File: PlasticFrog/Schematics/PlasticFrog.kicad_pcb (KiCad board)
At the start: 2 copper layers, 87.3 x 90.1 mm, 210 parts, among them J1 USB_A, J2 Conn_01x04, J3 Conn_01x05, U1 CH552T

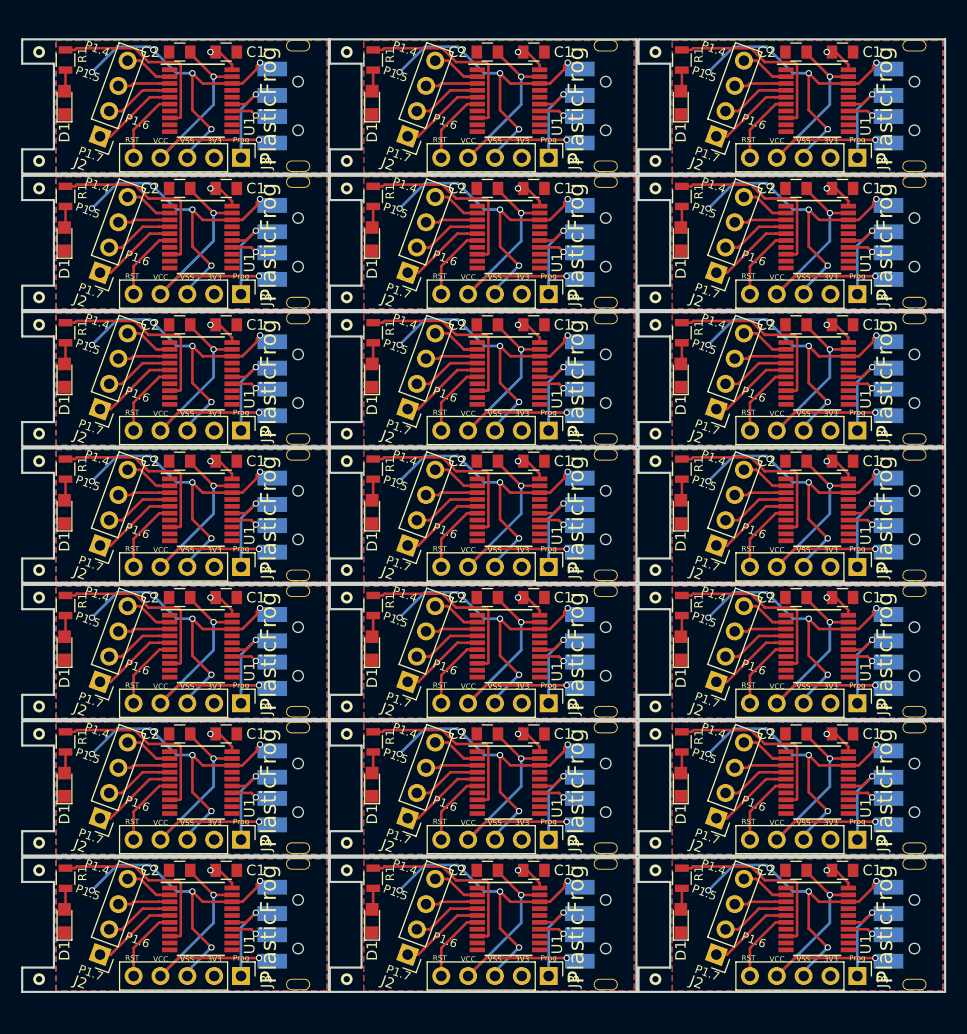
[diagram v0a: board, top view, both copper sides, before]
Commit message: Cant believe I had D+ and D- mixed...
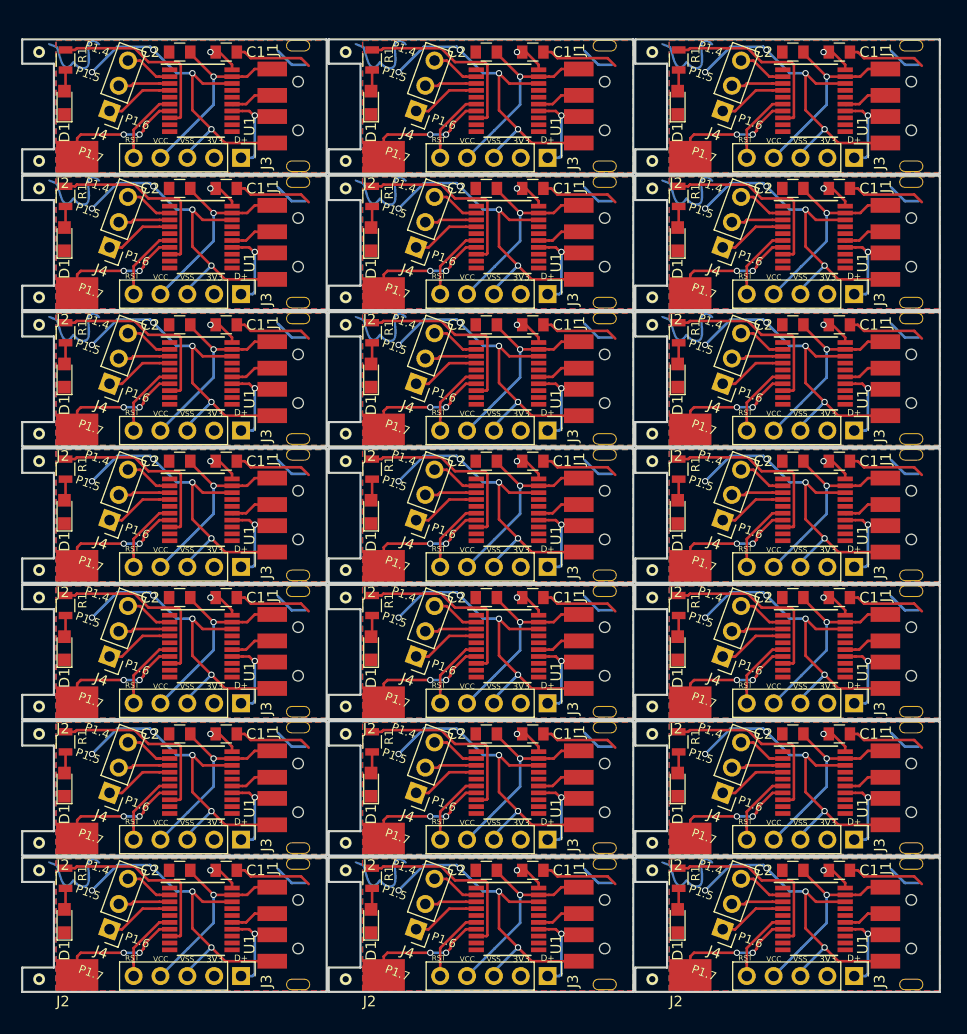
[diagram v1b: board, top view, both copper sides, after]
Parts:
- removed the ? at (185.4, 73.8)
- removed the ? at (185.4, 135.7)
- removed the ? at (185.4, 138.3)
- removed the ? at (185.4, 122.8)
- removed the ? at (185.4, 99.6)
- removed the ? at (185.4, 109.9)
- removed the ? at (156.2, 138.3)
- removed the ? at (156.2, 148.6)
- removed the ? at (156.2, 97.0)
- removed the ? at (156.2, 71.2)
- removed the ? at (156.2, 135.7)
- removed the ? at (185.4, 86.7)
- removed the ? at (156.2, 99.6)
- removed the ? at (156.2, 109.9)
- removed the ? at (156.2, 122.8)
- removed the ? at (156.2, 84.1)
- removed the ? at (156.2, 125.4)
- removed the ? at (156.2, 60.9)
- removed the ? at (156.2, 86.7)
- removed the ? at (156.2, 73.8)
- removed the ? at (156.2, 112.5)
- removed the ? at (185.4, 97.0)
- removed the ? at (185.4, 60.9)
- removed the ? at (185.4, 71.2)
- removed the ? at (185.4, 112.5)
- removed the ? at (185.4, 148.6)
- removed the ? at (185.4, 125.4)
- removed the ? at (185.4, 84.1)
- removed the C1 at (203.1, 112.5)
- removed the C1 at (173.9, 125.4)
- removed the C1 at (173.9, 112.5)
- removed the C1 at (173.9, 86.7)
- removed the C1 at (173.9, 73.8)
- removed the C1 at (173.9, 99.6)
- removed the C1 at (203.1, 125.4)
- removed the C1 at (203.1, 99.6)
- removed the C1 at (203.1, 86.7)
- removed the C1 at (203.1, 73.8)
- removed the C1 at (203.1, 60.9)
- removed the C1 at (203.1, 138.3)
- removed the C1 at (173.9, 138.3)
- removed the C1 at (173.9, 60.9)
- removed the C2 at (198.7, 86.7)
- removed the C2 at (169.5, 112.5)
- removed the C2 at (169.5, 73.8)
- removed the C2 at (169.5, 125.4)
- removed the C2 at (169.5, 99.6)
- removed the C2 at (169.5, 86.7)
- removed the C2 at (198.7, 99.6)
- removed the C2 at (198.7, 112.5)
- removed the C2 at (198.7, 60.9)
- removed the C2 at (198.7, 73.8)
- removed the C2 at (198.7, 138.3)
- removed the C2 at (198.7, 125.4)
- removed the C2 at (169.5, 138.3)
- removed the C2 at (169.5, 60.9)
- removed the D1 at (187.8, 117.3)
- removed the D1 at (158.6, 104.4)
- removed the D1 at (158.6, 91.5)
- removed the D1 at (158.6, 65.7)
- removed the D1 at (158.6, 78.6)
- removed the D1 at (158.6, 130.2)
- removed the D1 at (187.8, 130.2)
- removed the D1 at (187.8, 91.5)
- removed the D1 at (187.8, 143.1)
- removed the D1 at (187.8, 104.4)
- removed the D1 at (187.8, 78.6)
- removed the D1 at (187.8, 65.7)
- removed the D1 at (158.6, 117.3)
- removed the D1 at (158.6, 143.1)
- removed the J1 at (208.8, 117.6)
- removed the J1 at (179.6, 117.6)
- removed the J1 at (179.6, 104.7)
- removed the J1 at (179.6, 130.5)
- removed the J1 at (179.6, 78.9)
- removed the J1 at (179.6, 91.8)
- removed the J1 at (208.8, 91.8)
- removed the J1 at (208.8, 66.0)
- removed the J1 at (208.8, 143.4)
- removed the J1 at (208.8, 78.9)
- removed the J1 at (208.8, 104.7)
- removed the J1 at (208.8, 130.5)
- removed the J1 at (179.6, 66.0)
- removed the J1 at (179.6, 143.4)
- removed the J2 at (191.2, 81.8)
- removed the J2 at (162.0, 107.6)
- removed the J2 at (162.0, 120.5)
- removed the J2 at (162.0, 146.3)
- removed the J2 at (162.0, 94.7)
- removed the J2 at (162.0, 133.4)
- removed the J2 at (132.9, 81.8)
- removed the J2 at (132.9, 107.6)
- removed the J2 at (132.9, 94.7)
- removed the J2 at (132.9, 68.9)
- removed the J2 at (132.9, 120.5)
- removed the J2 at (191.2, 146.3)
- removed the J2 at (132.9, 133.4)
- removed the J2 at (132.9, 146.3)
- removed the J2 at (191.2, 120.5)
- removed the J2 at (191.2, 133.4)
- removed the J2 at (191.2, 107.6)
- removed the J2 at (191.2, 68.9)
- removed the J2 at (191.2, 94.7)
- removed the J2 at (162.0, 68.9)
- removed the J2 at (162.0, 81.8)
- removed the J3 at (204.5, 96.7)
- removed the J3 at (175.3, 70.9)
- removed the J3 at (175.3, 148.3)
- removed the J3 at (175.3, 109.6)
- removed the J3 at (175.3, 135.4)
- removed the J3 at (175.3, 96.7)
- removed the J3 at (204.5, 135.4)
- removed the J3 at (204.5, 70.9)
- removed the J3 at (204.5, 148.3)
- removed the J3 at (204.5, 109.6)
- removed the J3 at (204.5, 122.5)
- removed the J3 at (204.5, 83.8)
- removed the J3 at (175.3, 122.5)
- removed the J3 at (175.3, 83.8)
- removed the R1 at (187.9, 139.1)
- removed the R1 at (158.7, 74.5)
- removed the R1 at (158.7, 61.6)
- removed the R1 at (158.7, 113.2)
- removed the R1 at (158.7, 126.2)
- removed the R1 at (158.7, 100.3)
- removed the R1 at (187.9, 126.2)
- removed the R1 at (187.9, 100.3)
- removed the R1 at (187.9, 87.5)
- removed the R1 at (187.9, 61.6)
- removed the R1 at (187.9, 74.5)
- removed the R1 at (187.9, 113.2)
- removed the R1 at (158.7, 139.1)
- removed the R1 at (158.7, 87.5)
- removed the U1 at (200.7, 65.5)
- removed the U1 at (171.5, 104.2)
- removed the U1 at (171.5, 78.4)
- removed the U1 at (171.5, 65.5)
- removed the U1 at (171.5, 117.1)
- removed the U1 at (171.5, 130.0)
- removed the U1 at (200.7, 117.1)
- removed the U1 at (200.7, 142.9)
- removed the U1 at (200.7, 91.3)
- removed the U1 at (200.7, 130.0)
- removed the U1 at (200.7, 78.4)
- removed the U1 at (200.7, 104.2)
- removed the U1 at (171.5, 142.9)
- removed the U1 at (171.5, 91.3)
- added ?: , Wire_Pads:SolderWirePad_single_1mmDrill, F.Cu at (185.1, 125.4)
- added ?: , Wire_Pads:SolderWirePad_single_1mmDrill, F.Cu at (185.1, 73.8)
- added ?: , Wire_Pads:SolderWirePad_single_1mmDrill, F.Cu at (185.1, 122.8)
- added ?: , Wire_Pads:SolderWirePad_single_1mmDrill, F.Cu at (185.1, 138.3)
- added ?: , Wire_Pads:SolderWirePad_single_1mmDrill, F.Cu at (185.1, 84.1)
- added ?: , Wire_Pads:SolderWirePad_single_1mmDrill, F.Cu at (185.1, 97.0)
- added ?: , Wire_Pads:SolderWirePad_single_1mmDrill, F.Cu at (156.1, 148.6)
- added ?: , Wire_Pads:SolderWirePad_single_1mmDrill, F.Cu at (156.1, 138.3)
- added ?: , Wire_Pads:SolderWirePad_single_1mmDrill, F.Cu at (156.1, 99.6)
- added ?: , Wire_Pads:SolderWirePad_single_1mmDrill, F.Cu at (156.1, 112.5)
- added ?: , Wire_Pads:SolderWirePad_single_1mmDrill, F.Cu at (156.1, 86.7)
- added ?: , Wire_Pads:SolderWirePad_single_1mmDrill, F.Cu at (185.1, 135.7)
- added ?: , Wire_Pads:SolderWirePad_single_1mmDrill, F.Cu at (156.1, 97.0)
- added ?: , Wire_Pads:SolderWirePad_single_1mmDrill, F.Cu at (156.1, 122.8)
- added ?: , Wire_Pads:SolderWirePad_single_1mmDrill, F.Cu at (156.1, 125.4)
- added ?: , Wire_Pads:SolderWirePad_single_1mmDrill, F.Cu at (156.1, 135.7)
- added ?: , Wire_Pads:SolderWirePad_single_1mmDrill, F.Cu at (156.1, 109.9)
- added ?: , Wire_Pads:SolderWirePad_single_1mmDrill, F.Cu at (156.1, 71.2)
- added ?: , Wire_Pads:SolderWirePad_single_1mmDrill, F.Cu at (156.1, 60.9)
- added ?: , Wire_Pads:SolderWirePad_single_1mmDrill, F.Cu at (156.1, 84.1)
- added ?: , Wire_Pads:SolderWirePad_single_1mmDrill, F.Cu at (156.1, 73.8)
- added ?: , Wire_Pads:SolderWirePad_single_1mmDrill, F.Cu at (185.1, 148.6)
- added ?: , Wire_Pads:SolderWirePad_single_1mmDrill, F.Cu at (185.1, 109.9)
- added ?: , Wire_Pads:SolderWirePad_single_1mmDrill, F.Cu at (185.1, 71.2)
- added ?: , Wire_Pads:SolderWirePad_single_1mmDrill, F.Cu at (185.1, 86.7)
- added ?: , Wire_Pads:SolderWirePad_single_1mmDrill, F.Cu at (185.1, 99.6)
- added ?: , Wire_Pads:SolderWirePad_single_1mmDrill, F.Cu at (185.1, 112.5)
- added ?: , Wire_Pads:SolderWirePad_single_1mmDrill, F.Cu at (185.1, 60.9)
- added C1: 0.1uF, Capacitors_SMD:C_0805, F.Cu at (202.8, 125.4)
- added C1: 0.1uF, Capacitors_SMD:C_0805, F.Cu at (173.8, 86.7)
- added C1: 0.1uF, Capacitors_SMD:C_0805, F.Cu at (173.8, 138.3)
- added C1: 0.1uF, Capacitors_SMD:C_0805, F.Cu at (173.8, 99.6)
- added C1: 0.1uF, Capacitors_SMD:C_0805, F.Cu at (173.8, 60.9)
- added C1: 0.1uF, Capacitors_SMD:C_0805, F.Cu at (173.8, 125.4)
- added C1: 0.1uF, Capacitors_SMD:C_0805, F.Cu at (202.8, 112.5)
- added C1: 0.1uF, Capacitors_SMD:C_0805, F.Cu at (202.8, 60.9)
- added C1: 0.1uF, Capacitors_SMD:C_0805, F.Cu at (202.8, 73.8)
- added C1: 0.1uF, Capacitors_SMD:C_0805, F.Cu at (202.8, 138.3)
- added C1: 0.1uF, Capacitors_SMD:C_0805, F.Cu at (202.8, 86.7)
- added C1: 0.1uF, Capacitors_SMD:C_0805, F.Cu at (202.8, 99.6)
- added C1: 0.1uF, Capacitors_SMD:C_0805, F.Cu at (173.8, 73.8)
- added C1: 0.1uF, Capacitors_SMD:C_0805, F.Cu at (173.8, 112.5)
- added C2: 0.1uF, Capacitors_SMD:C_0805, F.Cu at (198.4, 99.6)
- added C2: 0.1uF, Capacitors_SMD:C_0805, F.Cu at (169.4, 138.3)
- added C2: 0.1uF, Capacitors_SMD:C_0805, F.Cu at (169.4, 125.4)
- added C2: 0.1uF, Capacitors_SMD:C_0805, F.Cu at (169.4, 112.5)
- added C2: 0.1uF, Capacitors_SMD:C_0805, F.Cu at (169.4, 60.9)
- added C2: 0.1uF, Capacitors_SMD:C_0805, F.Cu at (169.4, 73.8)
- added C2: 0.1uF, Capacitors_SMD:C_0805, F.Cu at (198.4, 138.3)
- added C2: 0.1uF, Capacitors_SMD:C_0805, F.Cu at (198.4, 112.5)
- added C2: 0.1uF, Capacitors_SMD:C_0805, F.Cu at (198.4, 73.8)
- added C2: 0.1uF, Capacitors_SMD:C_0805, F.Cu at (198.4, 125.4)
- added C2: 0.1uF, Capacitors_SMD:C_0805, F.Cu at (198.4, 60.9)
- added C2: 0.1uF, Capacitors_SMD:C_0805, F.Cu at (198.4, 86.7)
- added C2: 0.1uF, Capacitors_SMD:C_0805, F.Cu at (169.4, 99.6)
- added C2: 0.1uF, Capacitors_SMD:C_0805, F.Cu at (169.4, 86.7)
- added D1: LED, LEDs:LED_0805, F.Cu at (187.5, 104.4)
- added D1: LED, LEDs:LED_0805, F.Cu at (158.5, 130.2)
- added D1: LED, LEDs:LED_0805, F.Cu at (158.5, 117.3)
- added D1: LED, LEDs:LED_0805, F.Cu at (158.5, 91.5)
- added D1: LED, LEDs:LED_0805, F.Cu at (158.5, 65.7)
- added D1: LED, LEDs:LED_0805, F.Cu at (158.5, 104.4)
- added D1: LED, LEDs:LED_0805, F.Cu at (187.5, 143.1)
- added D1: LED, LEDs:LED_0805, F.Cu at (187.5, 65.7)
- added D1: LED, LEDs:LED_0805, F.Cu at (187.5, 130.2)
- added D1: LED, LEDs:LED_0805, F.Cu at (187.5, 78.6)
- added D1: LED, LEDs:LED_0805, F.Cu at (187.5, 117.3)
- added D1: LED, LEDs:LED_0805, F.Cu at (187.5, 91.5)
- added D1: LED, LEDs:LED_0805, F.Cu at (158.5, 78.6)
- added D1: LED, LEDs:LED_0805, F.Cu at (158.5, 143.1)
- added J1: USB_A, Connectors_USB:USB-A_Jing, F.Cu at (208.4, 78.9)
- added J1: USB_A, Connectors_USB:USB-A_Jing, F.Cu at (179.4, 91.8)
- added J1: USB_A, Connectors_USB:USB-A_Jing, F.Cu at (179.4, 130.5)
- added J1: USB_A, Connectors_USB:USB-A_Jing, F.Cu at (179.4, 117.6)
- added J1: USB_A, Connectors_USB:USB-A_Jing, F.Cu at (179.4, 66.0)
- added J1: USB_A, Connectors_USB:USB-A_Jing, F.Cu at (179.4, 78.9)
- added J1: USB_A, Connectors_USB:USB-A_Jing, F.Cu at (208.4, 117.6)
- added J1: USB_A, Connectors_USB:USB-A_Jing, F.Cu at (208.4, 143.4)
- added J1: USB_A, Connectors_USB:USB-A_Jing, F.Cu at (208.4, 104.7)
- added J1: USB_A, Connectors_USB:USB-A_Jing, F.Cu at (208.4, 91.8)
- added J1: USB_A, Connectors_USB:USB-A_Jing, F.Cu at (208.4, 66.0)
- added J1: USB_A, Connectors_USB:USB-A_Jing, F.Cu at (208.4, 130.5)
- added J1: USB_A, Connectors_USB:USB-A_Jing, F.Cu at (179.4, 104.7)
- added J1: USB_A, Connectors_USB:USB-A_Jing, F.Cu at (179.4, 143.4)
- added J2: Conn_01x01, Card:TouchPad_small, F.Cu at (188.7, 83.7)
- added J2: Conn_01x01, Card:TouchPad_small, F.Cu at (159.7, 83.7)
- added J2: Conn_01x01, Card:TouchPad_small, F.Cu at (159.7, 135.3)
- added J2: Conn_01x01, Card:TouchPad_small, F.Cu at (159.7, 122.4)
- added J2: Conn_01x01, Card:TouchPad_small, F.Cu at (159.7, 96.6)
- added J2: Conn_01x01, Card:TouchPad_small, F.Cu at (159.7, 109.5)
- added J2: Conn_01x01, Card:TouchPad_small, F.Cu at (130.7, 109.5)
- added J2: Conn_01x01, Card:TouchPad_small, F.Cu at (130.7, 122.4)
- added J2: Conn_01x01, Card:TouchPad_small, F.Cu at (130.7, 135.3)
- added J2: Conn_01x01, Card:TouchPad_small, F.Cu at (130.7, 96.6)
- added J2: Conn_01x01, Card:TouchPad_small, F.Cu at (130.7, 83.7)
- added J2: Conn_01x01, Card:TouchPad_small, F.Cu at (188.7, 148.2)
- added J2: Conn_01x01, Card:TouchPad_small, F.Cu at (130.7, 148.2)
- added J2: Conn_01x01, Card:TouchPad_small, F.Cu at (130.7, 70.8)
- added J2: Conn_01x01, Card:TouchPad_small, F.Cu at (188.7, 122.4)
- added J2: Conn_01x01, Card:TouchPad_small, F.Cu at (188.7, 70.8)
- added J2: Conn_01x01, Card:TouchPad_small, F.Cu at (188.7, 135.3)
- added J2: Conn_01x01, Card:TouchPad_small, F.Cu at (188.7, 109.5)
- added J2: Conn_01x01, Card:TouchPad_small, F.Cu at (188.7, 96.6)
- added J2: Conn_01x01, Card:TouchPad_small, F.Cu at (159.7, 148.2)
- added J2: Conn_01x01, Card:TouchPad_small, F.Cu at (159.7, 70.8)
- added J3: Conn_01x05, Pin_Headers:Pin_Header_Straight_1x05_Pitch2.54mm, F.Cu at (204.2, 83.8)
- added J3: Conn_01x05, Pin_Headers:Pin_Header_Straight_1x05_Pitch2.54mm, F.Cu at (175.2, 122.5)
- added J3: Conn_01x05, Pin_Headers:Pin_Header_Straight_1x05_Pitch2.54mm, F.Cu at (175.2, 135.4)
- added J3: Conn_01x05, Pin_Headers:Pin_Header_Straight_1x05_Pitch2.54mm, F.Cu at (175.2, 70.9)
- added J3: Conn_01x05, Pin_Headers:Pin_Header_Straight_1x05_Pitch2.54mm, F.Cu at (175.2, 96.7)
- added J3: Conn_01x05, Pin_Headers:Pin_Header_Straight_1x05_Pitch2.54mm, F.Cu at (175.2, 83.8)
- added J3: Conn_01x05, Pin_Headers:Pin_Header_Straight_1x05_Pitch2.54mm, F.Cu at (204.2, 109.6)
- added J3: Conn_01x05, Pin_Headers:Pin_Header_Straight_1x05_Pitch2.54mm, F.Cu at (204.2, 122.5)
- added J3: Conn_01x05, Pin_Headers:Pin_Header_Straight_1x05_Pitch2.54mm, F.Cu at (204.2, 70.9)
- added J3: Conn_01x05, Pin_Headers:Pin_Header_Straight_1x05_Pitch2.54mm, F.Cu at (204.2, 135.4)
- added J3: Conn_01x05, Pin_Headers:Pin_Header_Straight_1x05_Pitch2.54mm, F.Cu at (204.2, 96.7)
- added J3: Conn_01x05, Pin_Headers:Pin_Header_Straight_1x05_Pitch2.54mm, F.Cu at (204.2, 148.3)
- added J3: Conn_01x05, Pin_Headers:Pin_Header_Straight_1x05_Pitch2.54mm, F.Cu at (175.2, 109.6)
- added J3: Conn_01x05, Pin_Headers:Pin_Header_Straight_1x05_Pitch2.54mm, F.Cu at (175.2, 148.3)
- added J4: Conn_01x03, Pin_Headers:Pin_Header_Straight_1x03_Pitch2.54mm, F.Cu at (191.8, 105.2)
- added J4: Conn_01x03, Pin_Headers:Pin_Header_Straight_1x03_Pitch2.54mm, F.Cu at (162.8, 143.9)
- added J4: Conn_01x03, Pin_Headers:Pin_Header_Straight_1x03_Pitch2.54mm, F.Cu at (162.8, 66.5)
- added J4: Conn_01x03, Pin_Headers:Pin_Header_Straight_1x03_Pitch2.54mm, F.Cu at (162.8, 131.0)
- added J4: Conn_01x03, Pin_Headers:Pin_Header_Straight_1x03_Pitch2.54mm, F.Cu at (162.8, 105.2)
- added J4: Conn_01x03, Pin_Headers:Pin_Header_Straight_1x03_Pitch2.54mm, F.Cu at (162.8, 92.3)
- added J4: Conn_01x03, Pin_Headers:Pin_Header_Straight_1x03_Pitch2.54mm, F.Cu at (133.8, 118.1)
- added J4: Conn_01x03, Pin_Headers:Pin_Header_Straight_1x03_Pitch2.54mm, F.Cu at (133.8, 105.2)
- added J4: Conn_01x03, Pin_Headers:Pin_Header_Straight_1x03_Pitch2.54mm, F.Cu at (133.8, 131.0)
- added J4: Conn_01x03, Pin_Headers:Pin_Header_Straight_1x03_Pitch2.54mm, F.Cu at (133.8, 92.3)
- added J4: Conn_01x03, Pin_Headers:Pin_Header_Straight_1x03_Pitch2.54mm, F.Cu at (133.8, 79.4)
- added J4: Conn_01x03, Pin_Headers:Pin_Header_Straight_1x03_Pitch2.54mm, F.Cu at (191.8, 118.1)
- added J4: Conn_01x03, Pin_Headers:Pin_Header_Straight_1x03_Pitch2.54mm, F.Cu at (133.8, 143.9)
- added J4: Conn_01x03, Pin_Headers:Pin_Header_Straight_1x03_Pitch2.54mm, F.Cu at (133.8, 66.5)
- added J4: Conn_01x03, Pin_Headers:Pin_Header_Straight_1x03_Pitch2.54mm, F.Cu at (191.8, 79.4)
- added J4: Conn_01x03, Pin_Headers:Pin_Header_Straight_1x03_Pitch2.54mm, F.Cu at (191.8, 92.3)
- added J4: Conn_01x03, Pin_Headers:Pin_Header_Straight_1x03_Pitch2.54mm, F.Cu at (191.8, 66.5)
- added J4: Conn_01x03, Pin_Headers:Pin_Header_Straight_1x03_Pitch2.54mm, F.Cu at (191.8, 131.0)
- added J4: Conn_01x03, Pin_Headers:Pin_Header_Straight_1x03_Pitch2.54mm, F.Cu at (191.8, 143.9)
- added J4: Conn_01x03, Pin_Headers:Pin_Header_Straight_1x03_Pitch2.54mm, F.Cu at (162.8, 79.4)
- added J4: Conn_01x03, Pin_Headers:Pin_Header_Straight_1x03_Pitch2.54mm, F.Cu at (162.8, 118.1)
- added R1: 330ohm, Resistors_SMD:R_0805, F.Cu at (187.6, 100.3)
- added R1: 330ohm, Resistors_SMD:R_0805, F.Cu at (158.6, 100.3)
- added R1: 330ohm, Resistors_SMD:R_0805, F.Cu at (158.6, 87.5)
- added R1: 330ohm, Resistors_SMD:R_0805, F.Cu at (158.6, 113.2)
- added R1: 330ohm, Resistors_SMD:R_0805, F.Cu at (158.6, 126.2)
- added R1: 330ohm, Resistors_SMD:R_0805, F.Cu at (158.6, 61.6)
- added R1: 330ohm, Resistors_SMD:R_0805, F.Cu at (187.6, 74.5)
- added R1: 330ohm, Resistors_SMD:R_0805, F.Cu at (187.6, 113.2)
- added R1: 330ohm, Resistors_SMD:R_0805, F.Cu at (187.6, 87.5)
- added R1: 330ohm, Resistors_SMD:R_0805, F.Cu at (187.6, 126.2)
- added R1: 330ohm, Resistors_SMD:R_0805, F.Cu at (187.6, 61.6)
- added R1: 330ohm, Resistors_SMD:R_0805, F.Cu at (187.6, 139.1)
- added R1: 330ohm, Resistors_SMD:R_0805, F.Cu at (158.6, 74.5)
- added R1: 330ohm, Resistors_SMD:R_0805, F.Cu at (158.6, 139.1)
- added Ref**: Val**, NFCBuisness:W, B.Cu at (188.4, 88.0)
- added Ref**: Val**, NFCBuisness:W, B.Cu at (130.4, 75.1)
- added Ref**: Val**, NFCBuisness:W, B.Cu at (130.4, 139.6)
- added Ref**: Val**, NFCBuisness:W, B.Cu at (130.4, 62.2)
- added Ref**: Val**, NFCBuisness:W, B.Cu at (188.4, 75.1)
- added Ref**: Val**, NFCBuisness:W, B.Cu at (188.4, 139.6)
- added Ref**: Val**, NFCBuisness:W, B.Cu at (188.4, 62.2)
- added Ref**: Val**, NFCBuisness:W, B.Cu at (159.4, 88.0)
- added Ref**: Val**, NFCBuisness:W, B.Cu at (159.4, 139.6)
- added Ref**: Val**, NFCBuisness:W, B.Cu at (159.4, 62.2)
- added Ref**: Val**, NFCBuisness:W, B.Cu at (159.4, 75.1)
- added Ref**: Val**, NFCBuisness:W, B.Cu at (130.4, 88.0)
- added U1: CH552T, Housings_SSOP:TSSOP-20_4.4x6.5mm_Pitch0.65mm, F.Cu at (200.4, 117.1)
- added U1: CH552T, Housings_SSOP:TSSOP-20_4.4x6.5mm_Pitch0.65mm, F.Cu at (171.4, 117.1)
- added U1: CH552T, Housings_SSOP:TSSOP-20_4.4x6.5mm_Pitch0.65mm, F.Cu at (171.4, 104.2)
- added U1: CH552T, Housings_SSOP:TSSOP-20_4.4x6.5mm_Pitch0.65mm, F.Cu at (171.4, 91.3)
- added U1: CH552T, Housings_SSOP:TSSOP-20_4.4x6.5mm_Pitch0.65mm, F.Cu at (171.4, 78.4)
- added U1: CH552T, Housings_SSOP:TSSOP-20_4.4x6.5mm_Pitch0.65mm, F.Cu at (171.4, 65.5)
- added U1: CH552T, Housings_SSOP:TSSOP-20_4.4x6.5mm_Pitch0.65mm, F.Cu at (200.4, 142.9)
- added U1: CH552T, Housings_SSOP:TSSOP-20_4.4x6.5mm_Pitch0.65mm, F.Cu at (200.4, 65.5)
- added U1: CH552T, Housings_SSOP:TSSOP-20_4.4x6.5mm_Pitch0.65mm, F.Cu at (200.4, 130.0)
- added U1: CH552T, Housings_SSOP:TSSOP-20_4.4x6.5mm_Pitch0.65mm, F.Cu at (200.4, 78.4)
- added U1: CH552T, Housings_SSOP:TSSOP-20_4.4x6.5mm_Pitch0.65mm, F.Cu at (200.4, 104.2)
- added U1: CH552T, Housings_SSOP:TSSOP-20_4.4x6.5mm_Pitch0.65mm, F.Cu at (200.4, 91.3)
- added U1: CH552T, Housings_SSOP:TSSOP-20_4.4x6.5mm_Pitch0.65mm, F.Cu at (171.4, 142.9)
- added U1: CH552T, Housings_SSOP:TSSOP-20_4.4x6.5mm_Pitch0.65mm, F.Cu at (171.4, 130.0)
- J1 (x7): moved to F.Cu
- turned J1 to 270 degrees (x7)
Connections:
- net Net-(U1-Pad7) renamed P1.0
- net P1.7 renamed Net-(U1-Pad5)
- U1 pad 14: D- -> D+ (x7)
- U1 pad 15: D+ -> D- (x7)
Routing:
- net P1.0: track 0.00 -> 247.2 mm, vias 0 -> 42
- net VSS: track 609.4 -> 819.0 mm, vias 105 -> 84
- net Net-(U1-Pad5): track 170.5 -> 0.00 mm
- net VCC: track 520.1 -> 395.7 mm, vias 42 -> 21
- net (no net): track 0.00 -> 65.9 mm
- net D-: track 84.4 -> 89.2 mm, vias 21 -> 0
- net D+: track 258.6 -> 261.3 mm
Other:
- board size 87.3 x 90.1 mm -> 86.8 x 90.1 mm
- board text added: "D+"
- board text added: "V2"
- board text removed: "Prog"
